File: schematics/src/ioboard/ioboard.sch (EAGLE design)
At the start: 31 parts

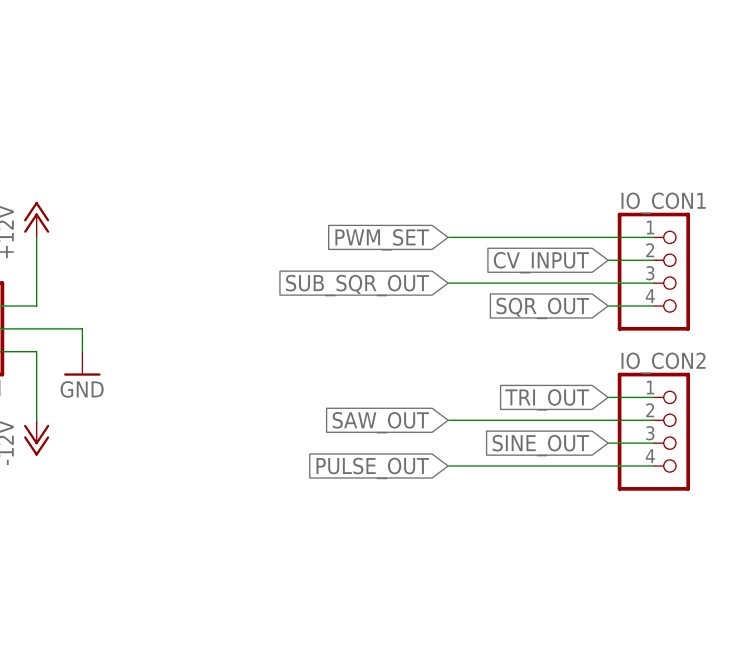
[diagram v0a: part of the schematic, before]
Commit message: Updated Schematics, Fixed Power Socket orientation
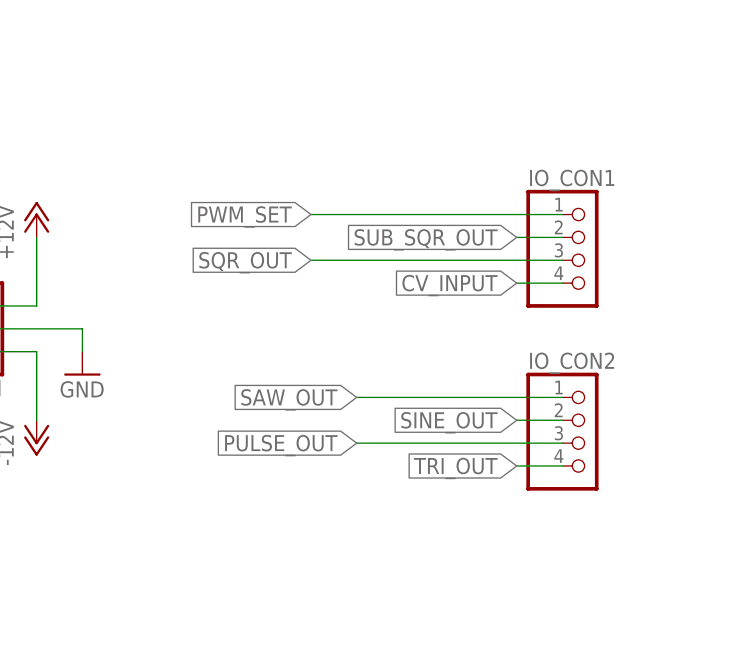
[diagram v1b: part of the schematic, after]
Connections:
- net CV_INPUT: now also IO_CON1.4; no longer IO_CON1.2
- net PULSE_OUT: now also IO_CON2.3; no longer IO_CON2.4
- net SAW_OUT: now also IO_CON2.1; no longer IO_CON2.2
- net SINE_OUT: now also IO_CON2.2; no longer IO_CON2.3
- net SQR_OUT: now also IO_CON1.3; no longer IO_CON1.4
- net SUB_SQR_OUT: now also IO_CON1.2; no longer IO_CON1.3
- net TRI_OUT: now also IO_CON2.4; no longer IO_CON2.1
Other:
- moved on the sheet: IO_CON1, IO_CON2
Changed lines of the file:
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@@
 <part name="GND11" library="supply1" deviceset="GND" device=""/>
 <part name="R1" library="rcl" library_urn="urn:adsk.eagle:library:334" deviceset="R-US_" device="0207/7" package3d_urn="urn:adsk.eagle:package:23493/2" value="100k"/>
-<part name="IO_CON2" library="pinhead" library_urn="urn:adsk.eagle:library:325" deviceset="PINHD-1X4" device="" package3d_urn="urn:adsk.eagle:package:22407/2"/>
-<part name="IO_CON1" library="pinhead" library_urn="urn:adsk.eagle:library:325" deviceset="PINHD-1X4" device="" package3d_urn="urn:adsk.eagle:package:22407/2"/>
 <part name="R2" library="rcl" library_urn="urn:adsk.eagle:library:334" deviceset="R-US_" device="0207/7" package3d_urn="urn:adsk.eagle:package:23493/2" value="12k"/>
 <part name="R3" library="rcl" library_urn="urn:adsk.eagle:library:334" deviceset="R-US_" device="0207/7" package3d_urn="urn:adsk.eagle:package:23493/2" value="12k"/>
 <part name="R11" library="rcl" library_urn="urn:adsk.eagle:library:334" deviceset="R-US_" device="0207/7" package3d_urn="urn:adsk.eagle:package:23493/2" value="1k"/>
+<part name="IO_CON2" library="pinhead" library_urn="urn:adsk.eagle:library:325" deviceset="PINHD-1X4" device="" package3d_urn="urn:adsk.eagle:package:22407/2"/>
+<part name="IO_CON1" library="pinhead" library_urn="urn:adsk.eagle:library:325" deviceset="PINHD-1X4" device="" package3d_urn="urn:adsk.eagle:package:22407/2"/>
 </parts>
 <sheets>
@@
 <attribute name="VALUE" x="123.19" y="75.438" size="1.778" layer="96"/>
 </instance>
-<instance part="IO_CON2" gate="A" x="292.1" y="48.26" smashed="yes">
-<attribute name="NAME" x="285.75" y="56.515" size="1.778" layer="95"/>
-<attribute name="VALUE" x="285.75" y="40.64" size="1.778" layer="96"/>
-</instance>
-<instance part="IO_CON1" gate="A" x="292.1" y="66.04" smashed="yes">
-<attribute name="NAME" x="285.75" y="74.295" size="1.778" layer="95"/>
-<attribute name="VALUE" x="285.75" y="58.42" size="1.778" layer="96"/>
-</instance>
 <instance part="R2" gate="G$1" x="101.6" y="68.58" smashed="yes" rot="R90">
 <attribute name="NAME" x="100.1014" y="64.77" size="1.778" layer="95" rot="R90"/>
@@
 <attribute name="NAME" x="257.81" y="143.7386" size="1.778" layer="95"/>
 <attribute name="VALUE" x="257.81" y="138.938" size="1.778" layer="96"/>
+</instance>
+<instance part="IO_CON2" gate="A" x="281.94" y="48.26" smashed="yes">
+<attribute name="NAME" x="275.59" y="56.515" size="1.778" layer="95"/>
+<attribute name="VALUE" x="275.59" y="40.64" size="1.778" layer="96"/>
+</instance>
+<instance part="IO_CON1" gate="A" x="281.94" y="68.58" smashed="yes">
+<attribute name="NAME" x="275.59" y="76.835" size="1.778" layer="95"/>
+<attribute name="VALUE" x="275.59" y="60.96" size="1.778" layer="96"/>
 </instance>
 </instances>
@@
 </segment>
 <segment>
-<wire x1="289.56" y1="68.58" x2="284.48" y2="68.58" width="0.1524" layer="91"/>
-<label x="284.48" y="68.58" size="1.778" layer="95" rot="R180" xref="yes"/>
-<pinref part="IO_CON1" gate="A" pin="2"/>
+<label x="274.32" y="66.04" size="1.778" layer="95" rot="R180" xref="yes"/>
+<wire x1="279.4" y1="66.04" x2="274.32" y2="66.04" width="0.1524" layer="91"/>
+<pinref part="IO_CON1" gate="A" pin="4"/>
 </segment>
 </net>
@@
 </segment>
 <segment>
-<wire x1="289.56" y1="63.5" x2="284.48" y2="63.5" width="0.1524" layer="91"/>
-<label x="284.48" y="63.5" size="1.778" layer="95" rot="R180" xref="yes"/>
-<pinref part="IO_CON1" gate="A" pin="4"/>
+<label x="251.46" y="68.58" size="1.778" layer="95" rot="R180" xref="yes"/>
+<wire x1="279.4" y1="68.58" x2="251.46" y2="68.58" width="0.1524" layer="91"/>
+<pinref part="IO_CON1" gate="A" pin="3"/>
 </segment>
 </net>
@@
 </segment>
 <segment>
-<wire x1="289.56" y1="66.04" x2="266.7" y2="66.04" width="0.1524" layer="91"/>
-<label x="266.7" y="66.04" size="1.778" layer="95" rot="R180" xref="yes"/>
-<pinref part="IO_CON1" gate="A" pin="3"/>
+<label x="274.32" y="71.12" size="1.778" layer="95" rot="R180" xref="yes"/>
+<wire x1="279.4" y1="71.12" x2="274.32" y2="71.12" width="0.1524" layer="91"/>
+<pinref part="IO_CON1" gate="A" pin="2"/>
 </segment>
 </net>
@@
 </segment>
 <segment>
-<wire x1="289.56" y1="50.8" x2="266.7" y2="50.8" width="0.1524" layer="91"/>
-<label x="266.7" y="50.8" size="1.778" layer="95" rot="R180" xref="yes"/>
-<pinref part="IO_CON2" gate="A" pin="2"/>
+<label x="256.54" y="53.34" size="1.778" layer="95" rot="R180" xref="yes"/>
+<wire x1="279.4" y1="53.34" x2="256.54" y2="53.34" width="0.1524" layer="91"/>
+<pinref part="IO_CON2" gate="A" pin="1"/>
 </segment>
 </net>
@@
 </segment>
 <segment>
-<wire x1="289.56" y1="53.34" x2="284.48" y2="53.34" width="0.1524" layer="91"/>
-<label x="284.48" y="53.34" size="1.778" layer="95" rot="R180" xref="yes"/>
-<pinref part="IO_CON2" gate="A" pin="1"/>
+<label x="274.32" y="45.72" size="1.778" layer="95" rot="R180" xref="yes"/>
+<wire x1="279.4" y1="45.72" x2="274.32" y2="45.72" width="0.1524" layer="91"/>
+<pinref part="IO_CON2" gate="A" pin="4"/>
 </segment>
 </net>
 <net name="PULSE_OUT" class="0">
-<segment>
-<pinref part="IO_CON2" gate="A" pin="4"/>
-<wire x1="289.56" y1="45.72" x2="266.7" y2="45.72" width="0.1524" layer="91"/>
-<label x="266.7" y="45.72" size="1.778" layer="95" rot="R180" xref="yes"/>
-</segment>
 <segment>
 <pinref part="R11" gate="G$1" pin="1"/>
@@
 <label x="251.46" y="142.24" size="1.778" layer="95" rot="R180" xref="yes"/>
 </segment>
+<segment>
+<label x="256.54" y="48.26" size="1.778" layer="95" rot="R180" xref="yes"/>
+<wire x1="279.4" y1="48.26" x2="256.54" y2="48.26" width="0.1524" layer="91"/>
+<pinref part="IO_CON2" gate="A" pin="3"/>
+</segment>
 </net>
 <net name="SINE_OUT" class="0">
@@
 </segment>
 <segment>
-<wire x1="289.56" y1="48.26" x2="284.48" y2="48.26" width="0.1524" layer="91"/>
-<label x="284.48" y="48.26" size="1.778" layer="95" rot="R180" xref="yes"/>
-<pinref part="IO_CON2" gate="A" pin="3"/>
+<label x="274.32" y="50.8" size="1.778" layer="95" rot="R180" xref="yes"/>
+<wire x1="279.4" y1="50.8" x2="274.32" y2="50.8" width="0.1524" layer="91"/>
+<pinref part="IO_CON2" gate="A" pin="2"/>
 </segment>
 </net>
@@
 </segment>
 <segment>
+<label x="251.46" y="73.66" size="1.778" layer="95" rot="R180" xref="yes"/>
+<wire x1="279.4" y1="73.66" x2="251.46" y2="73.66" width="0.1524" layer="91"/>
 <pinref part="IO_CON1" gate="A" pin="1"/>
-<wire x1="289.56" y1="71.12" x2="266.7" y2="71.12" width="0.1524" layer="91"/>
-<label x="266.7" y="71.12" size="1.778" layer="95" rot="R180" xref="yes"/>
-</segment>
-</net>
+</segment>
+</net>
